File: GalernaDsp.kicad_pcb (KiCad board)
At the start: 4 copper layers, 121 x 121 mm, 124 parts, among them CN100 HX JN1.27-2X5 TP H4.9, J100 DM3CS-SF, J200 Headphones, J201 AudioInput, J202 AudioOutput, J300 USB_C_Receptacle_USB2.0_16P, SW400 100SP1T1B4M2QE, SW401 100SP1T1B4M2QE, U100 SW_RUN, U101 STM32F405RGTx, U200 WM8731SEDS, U201 TPA6110A2DGN, U300 USBLC6-2SC6, U301 TLV62569DBV, U302 SPX3819M5-L-3-3, U400 CD4051BM, X100 X1E000210127000G

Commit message: All DRC fixed
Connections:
- J300 pad S1: unconnected-(J300-SHIELD-PadS1)_2 -> GND
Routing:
- net GND: vias 130 -> 150
- net +3V3A: vias 6 -> 3

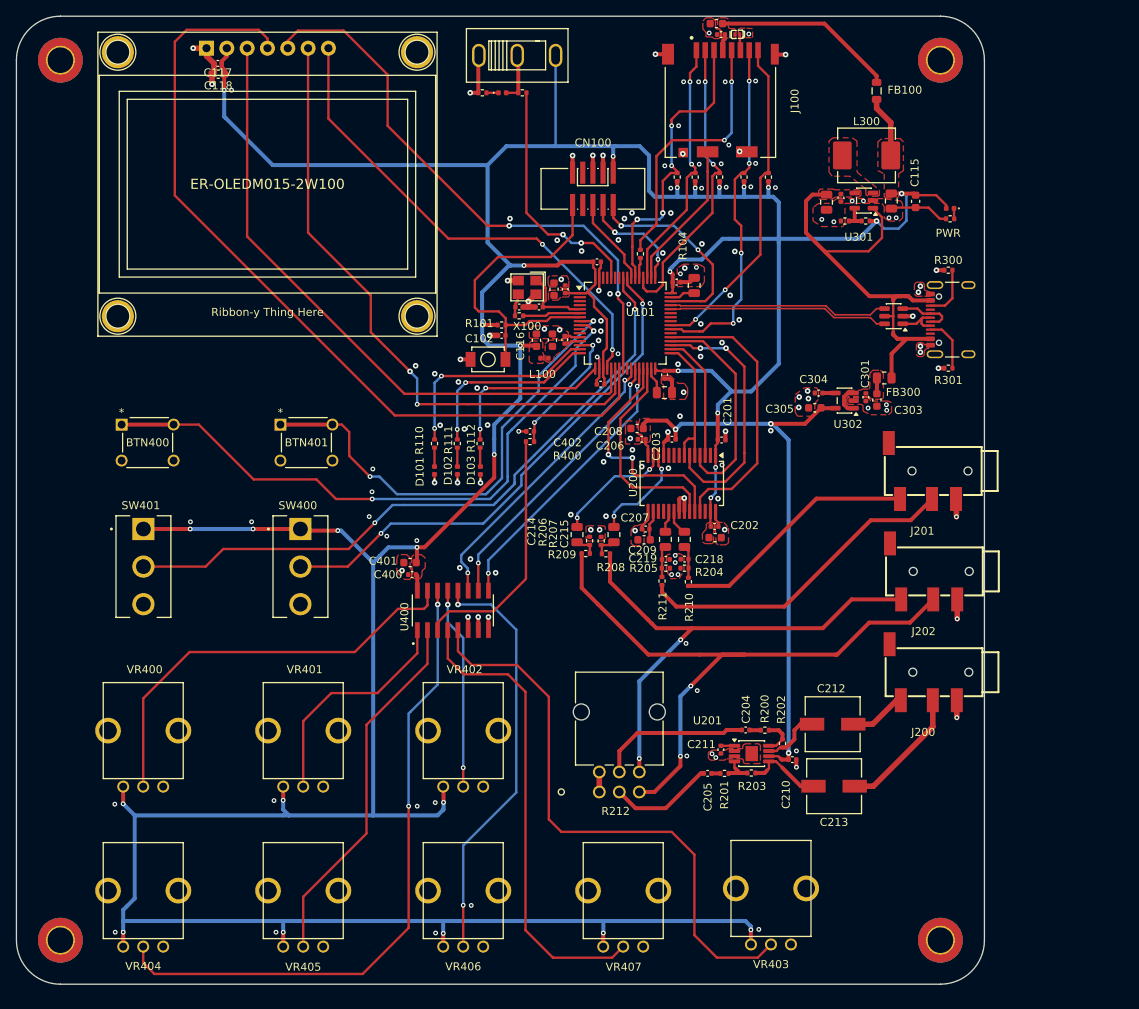
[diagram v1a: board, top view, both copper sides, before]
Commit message: Codec updated to ES8388 on schematic
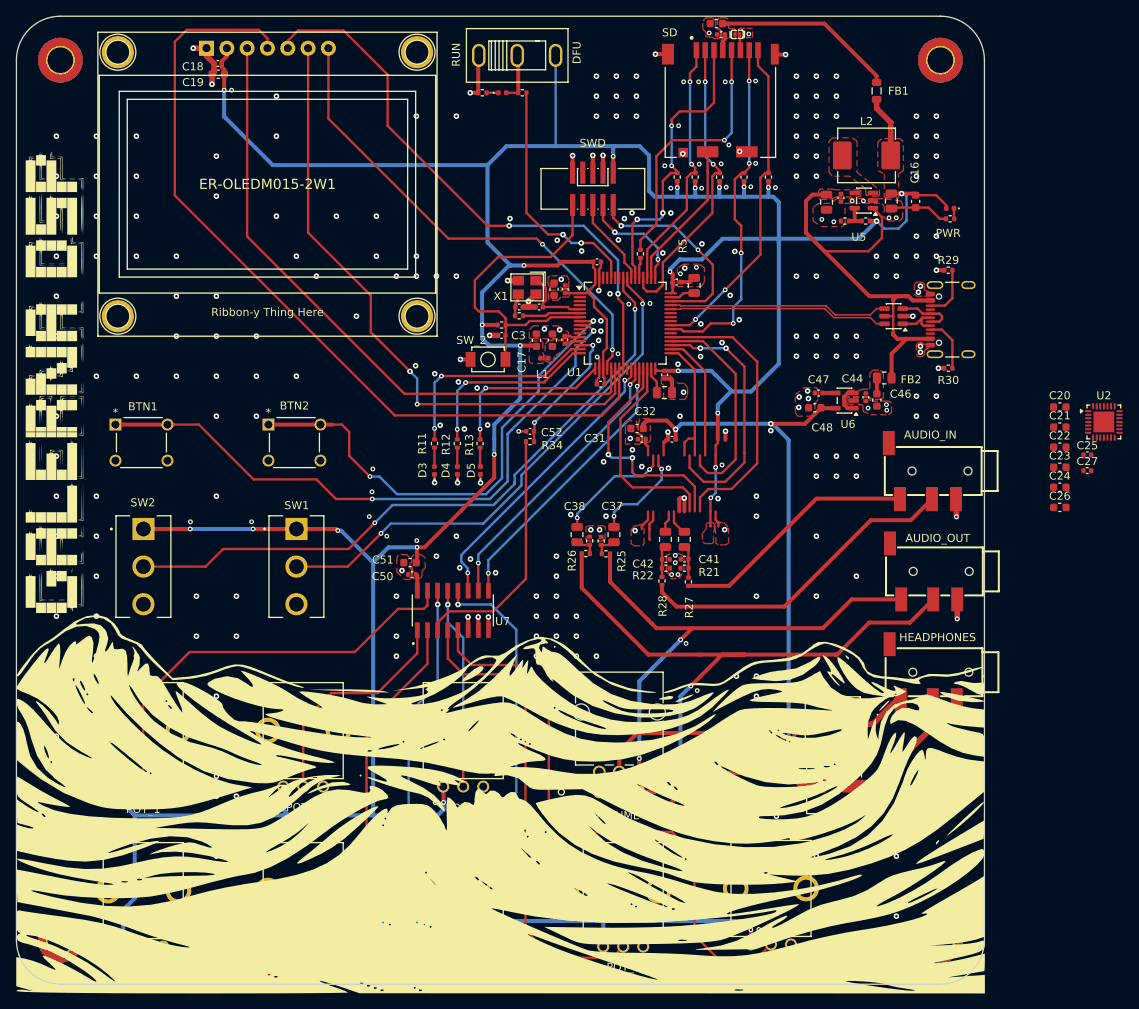
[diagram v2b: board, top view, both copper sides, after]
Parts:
- removed C200, C209: 10u, Capacitor_SMD:C_0603_1608Metric
- removed C201, C202, C207: 100n, Capacitor_SMD:C_0402_1005Metric
- removed U200: WM8731SEDS, Package_SO:SSOP-28_5.3x10.2mm_P0.65mm
- added C20: 10u, Capacitor_SMD:C_0603_1608Metric, F.Cu at (253.9, 83.3)
- added C21: 100n, Capacitor_SMD:C_0603_1608Metric, F.Cu at (253.9, 85.9)
- added C22: 10u, Capacitor_SMD:C_0603_1608Metric, F.Cu at (253.9, 88.4)
- added C23: 10u, Capacitor_SMD:C_0603_1608Metric, F.Cu at (253.9, 90.9)
- added C24: 10u, Capacitor_SMD:C_0603_1608Metric, F.Cu at (253.9, 93.4)
- added C25: 100n, Capacitor_SMD:C_0402_1005Metric, F.Cu at (257.4, 89.3)
- added C26: 100n, Capacitor_SMD:C_0603_1608Metric, F.Cu at (253.9, 95.9)
- added C27: 100n, Capacitor_SMD:C_0402_1005Metric, F.Cu at (257.4, 91.3)
- added G***: LOGO, Galerna:waves, F.Cu at (184.0, 122.8)
- added G***: LOGO, Galerna:Logo, F.Cu at (129.2, 79.9)
- added U2: ES8388, Package_DFN_QFN:QFN-28-1EP_4x4mm_P0.45mm_EP2.6x2.6mm, F.Cu at (259.4, 85.2)
- J2: renamed from J200; value Headphones -> HEADPHONES
- J3: renamed from J201; value AudioInput -> AUDIO_IN
- J4: renamed from J202; value AudioOutput -> AUDIO_OUT
- SW_1: renamed from U100; value SW_RUN -> BOOT_MODE
- moved BTN2 1.50 mm to (161.5, 90.0)
- moved BTN1 0.77 mm to (142.4, 90.0)
- moved SW1 0.50 mm to (158.5, 103.3)
- renumbered BTN400 to BTN1, BTN401 to BTN2, C100 to C1, C109 to C10, C110 to C11, C111 to C12, C112 to C13, C113 to C14, C114 to C15, C115 to C16, C116 to C17, C117 to C18, C118 to C19, C101 to C2, C203 to C28, C204 to C29, C102 to C3, C205 to C30, C206 to C31, C208 to C32, C210 to C33, C211 to C34, C212 to C35, C213 to C36, C214 to C37, C215 to C38, C216 to C39, C103 to C4, C217 to C40, C218 to C41, C219 to C42, C300 to C43, C301 to C44, C302 to C45, C303 to C46, C304 to C47, C305 to C48, C306 to C49, C104 to C5, C400 to C50, C401 to C51, C402 to C52, C105 to C6, C106 to C7, C107 to C8, C108 to C9, CN100 to CN1, D100 to D1, D104 to D2, D101 to D3, D102 to D4, D103 to D5, D300 to D6, ER-OLEDM015-2W100 to ER-OLEDM015-2W1, FB100 to FB1, FB300 to FB2, H000 to H1, H001 to H2, H002 to H3, H003 to H4, J100 to J1, J300 to J5, L100 to L1, L300 to L2, VR400 to POT_1, VR401 to POT_2, VR402 to POT_3, VR403 to POT_4, VR404 to POT_5, VR405 to POT_6, VR406 to POT_7, VR407 to POT_8, R100 to R1, R109 to R10, R110 to R11, R111 to R12, R112 to R13, R212 to R16, R200 to R17, R201 to R18, R202 to R19, R101 to R2, R203 to R20, R204 to R21, R205 to R22, R206 to R23, R207 to R24, R208 to R25, R209 to R26, R210 to R27, R211 to R28, R300 to R29, R102 to R3, R301 to R30, R302 to R31, R303 to R32, R304 to R33, R400 to R34, R103 to R4, R104 to R5, R105 to R6, R106 to R7, R107 to R8, R108 to R9, SW400 to SW1, SW401 to SW2, SW_100 to SW_2, U101 to U1, U201 to U3, U300 to U4, U301 to U5, U302 to U6, U400 to U7, X100 to X1
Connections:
- net SW_0 renamed SW_2
- net SW_1 renamed SW_3
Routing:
- net Net-(U200-VMID): track 3.79 -> 0.00 mm
- net Net-(U2-VMID): track 0.00 -> 3.79 mm
- net PUSH_BTN_1: track 60.0 -> 61.5 mm
- net +3V3: track 550.2 -> 550.9 mm
- net GND: vias 150 -> 339
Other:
- board text added: "DFU"
- board text added: "GALERNA. REV A. 04/2026"
- board text added: "RUN"
- board text added: "SD"
- board text added: "SWD"
- board text added: "VOLUME"

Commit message: ES8388 placed
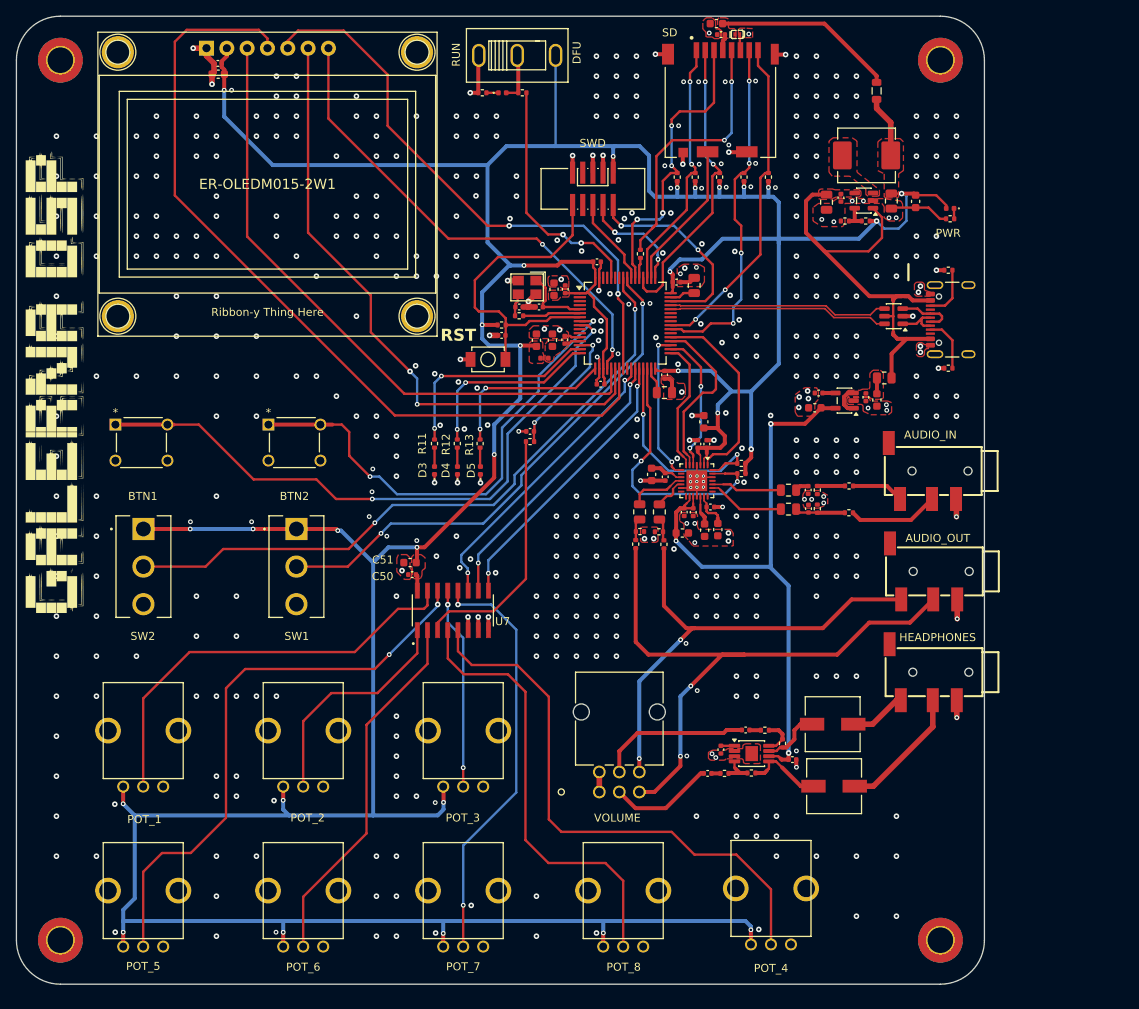
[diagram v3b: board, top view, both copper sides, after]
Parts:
- removed the G*** at (184.0, 122.8)
- added R14: 4k7, Resistor_SMD:R_0402_1005Metric, F.Cu at (214.1, 91.7)
- added R15: 4k7, Resistor_SMD:R_0402_1005Metric, F.Cu at (214.1, 90.4)
- C21, C26: footprint Capacitor_SMD:C_0603_1608Metric -> Capacitor_SMD:C_0402_1005Metric
- U2: footprint Package_DFN_QFN:QFN-28-1EP_4x4mm_P0.45mm_EP2.6x2.6mm -> Galerna:ES8388
- moved C20 51.7 mm to (202.9, 91.8), turned to -90 degrees
- moved U2 51.4 mm to (208.6, 92.6), turned to -90 degrees
- moved C21 49.7 mm to (204.6, 92.1), turned to -90 degrees
- moved C25 48.7 mm to (208.7, 88.0), turned to 90 degrees
- moved C27 47.7 mm to (209.8, 88.0), turned to 90 degrees
- moved C22 45.6 mm to (209.5, 98.8), turned to -90 degrees
- moved C23 44.9 mm to (209.4, 85.2), turned to 90 degrees
- moved C26 43.7 mm to (210.2, 95.8)
- moved C24 43.1 mm to (211.2, 98.7), turned to -90 degrees
- moved R28 24.9 mm to (227.6, 96.6), turned to 180 degrees
- moved R27 23.4 mm to (227.6, 93.2), turned to 180 degrees
- moved R22 20.3 mm to (223.6, 96.1), turned to -90 degrees
- moved R21 19.3 mm to (223.6, 93.7), turned to 90 degrees
- moved C42 18.9 mm to (222.5, 96.1), turned to 90 degrees
- moved C41 17.7 mm to (222.5, 93.7), turned to -90 degrees
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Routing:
- net /[2] Audio/AUDIO_R_IN: track 41.0 -> 11.3 mm
- net /[2] Audio/AUDIO_L_IN: track 31.0 -> 6.54 mm
- net CODEC_I2S_SDI: track 32.5 -> 18.8 mm
- net CODEC_I2S_MCK: track 35.5 -> 24.5 mm
- net /[3] Input Control/POT_2_CTL: track 81.7 -> 71.2 mm
- net +3V3: track 550.9 -> 560.7 mm, vias 30 -> 29
- net /[2] Audio/CODEC_L_OUT: track 12.7 -> 4.20 mm, vias 2 -> 0
- net /[2] Audio/CODEC_R_OUT: track 14.9 -> 7.17 mm, vias 2 -> 0
- net CODEC_I2C_SDA: track 26.5 -> 34.1 mm, vias 0 -> 2
- net /[2] Audio/CODEC_R_IN: track 2.73 -> 9.65 mm
- net GND: track 87.5 -> 94.1 mm, vias 339 -> 516
- net /[2] Audio/CODEC_L_IN: track 3.03 -> 8.86 mm
- net CODEC_I2S_SD: track 27.3 -> 21.6 mm
- net Net-(U2-VREF): track 0.00 -> 4.17 mm
- net /[2] Audio/AUDIO_L_OUT: track 64.5 -> 60.5 mm
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- removed copper zone on F.Cu, net +3V3A
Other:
- board text added: "RST"

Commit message: fillin info in parts
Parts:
- C21, C26: footprint Capacitor_SMD:C_0402_1005Metric -> Capacitor_SMD:C_0603_1608Metric
- R1, R34: value 1K -> 1k
- R3: value 10K -> 10k

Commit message: JLC order
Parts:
- removed the G*** at (129.2, 79.9)
- removed L1: 10n, Inductor_SMD:L_0402_1005Metric
- added FB3: 120@100Mhz, Resistor_SMD:R_0603_1608Metric, F.Cu at (189.5, 77.1)
- added G***: LOGO, Galerna:ola-4, F.Cu at (128.8, 46.2)
- added G***: LOGO, Galerna:ola-4, F.Cu at (191.1, 46.8)
- added G***: LOGO, Galerna:ola-4, F.Cu at (232.4, 37.4)
- added G***: LOGO, Galerna:ola-4, F.Cu at (231.7, 142.0)
- added G***: LOGO, Galerna:ola-4, F.Cu at (172.0, 135.2)
- added G***: LOGO, Galerna:GalernaLogo, F.Cu at (128.2, 83.2)
- added G***: LOGO, Galerna:ola-4, F.Cu at (220.1, 107.8)
- added G***: LOGO, Galerna:ola-4, F.Cu at (193.2, 88.8)
- added G***: LOGO, Galerna:ola-4, F.Cu at (151.4, 81.4)
- C21, C26: footprint Capacitor_SMD:C_0603_1608Metric -> Capacitor_SMD:C_0402_1005Metric
- C29, C30: value 470n -> 1u
- D1: footprint LED_SMD:LED_0402_1005Metric -> LED_SMD:LED_0603_1608Metric
- D3, D4, D5: value BLUE LED -> YELLOW_LED; footprint LED_SMD:LED_0402_1005Metric -> LED_SMD:LED_0603_1608Metric
- D6: footprint LED_SMD:LED_0402_1005Metric -> LED_SMD:LED_0805_2012Metric
- R11, R12, R13: value 330 -> 1k
- R21, R22: value 220k -> 200k
- moved D3 1.73 mm to (174.1, 91.0)
- moved R11 1.70 mm to (174.1, 88.1)
- moved D6 1.62 mm to (239.7, 57.0)
- moved D4 1.61 mm to (177.0, 91.0)
- moved R12 1.61 mm to (177.0, 88.2)
- moved R1 1.42 mm to (180.3, 44.1)
- moved D5 1.34 mm to (180.2, 90.9)
- moved R13 1.27 mm to (180.2, 88.1)
- moved D1 0.77 mm to (183.5, 44.1)
- moved R33 0.75 mm to (240.2, 59.1)
- moved C15 0.38 mm to (190.3, 74.7)
- moved C17 0.31 mm to (188.3, 74.7)
- moved C13 0.21 mm to (191.9, 74.8)
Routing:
- net GND: track 94.1 -> 88.7 mm, vias 516 -> 508
- net /[1] MCU/LED_1: track 23.3 -> 24.8 mm
- net /[1] MCU/LED_0: track 27.0 -> 28.3 mm
- net PUSH_BTN_1: track 61.5 -> 62.7 mm
- net Net-(C39-Pad1): track 5.18 -> 6.33 mm
- net +3V3: track 560.7 -> 559.6 mm
- net /[1] MCU/LED_2: track 21.5 -> 22.5 mm
- net Net-(D6-K): track 1.31 -> 2.29 mm
- net Net-(D3-A): track 2.37 -> 1.58 mm
- net Net-(D5-A): track 2.39 -> 1.63 mm
- net Net-(D4-A): track 2.38 -> 1.71 mm
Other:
- board text added: "+"
- board text added: "GALERNA. REV A. 06/2026"
- board text removed: "GALERNA. REV A. 04/2026"
